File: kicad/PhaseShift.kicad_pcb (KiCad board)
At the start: 2 copper layers, 66.4 x 128.6 mm, 56 parts

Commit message: small tweak
- pogo pin
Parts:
- moved POGO1 0.12 mm to (175.1, 95.5)
- moved POGO2 0.12 mm to (233.9, 95.5)
- moved POGO3 0.12 mm to (175.1, 142.4)
- moved POGO4 0.12 mm to (233.9, 142.4)
- moved POGO5 0.12 mm to (175.1, 182.0)
- moved POGO6 0.12 mm to (233.9, 182.0)
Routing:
- net ROW12: track 180.7 -> 185.0 mm
- net COL0: track 172.6 -> 171.7 mm
- net ROW14: track 137.8 -> 138.5 mm
- net COL2: track 176.9 -> 176.3 mm
- net GND: vias 2 -> 6

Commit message: 202508.04
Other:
- board text added: "OmniCode:9001 - 202508.04"
- board text removed: "OmniCode:9001 - 202507.22"

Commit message: tweaked zone (#22)
* small tweak

* removed isolated copper islands
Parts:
- turned POGO1 to -90 degrees
- turned POGO2 to 90 degrees
- turned POGO3 to -90 degrees
- turned POGO4 to 90 degrees
- turned POGO5 to -90 degrees
- turned POGO6 to 90 degrees
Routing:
- net SCR: track 75.6 -> 71.4 mm
- net COL2: track 176.3 -> 178.8 mm, vias 3 -> 2
- net NUM: track 62.7 -> 64.7 mm
- net ROW12: track 185.0 -> 186.8 mm
- net Net-(L7-DIN): track 29.8 -> 31.5 mm
- net Net-(L10-DOUT): track 47.8 -> 46.2 mm
- net +5V: track 316.8 -> 317.9 mm, vias 4 -> 7
- net COL1: track 184.0 -> 184.9 mm
- net COL0: track 171.7 -> 172.6 mm
- net RGB_TO_RIGHT: track 44.8 -> 44.1 mm
- net Net-(D3-A): track 5.95 -> 5.44 mm
- net GND: vias 6 -> 7

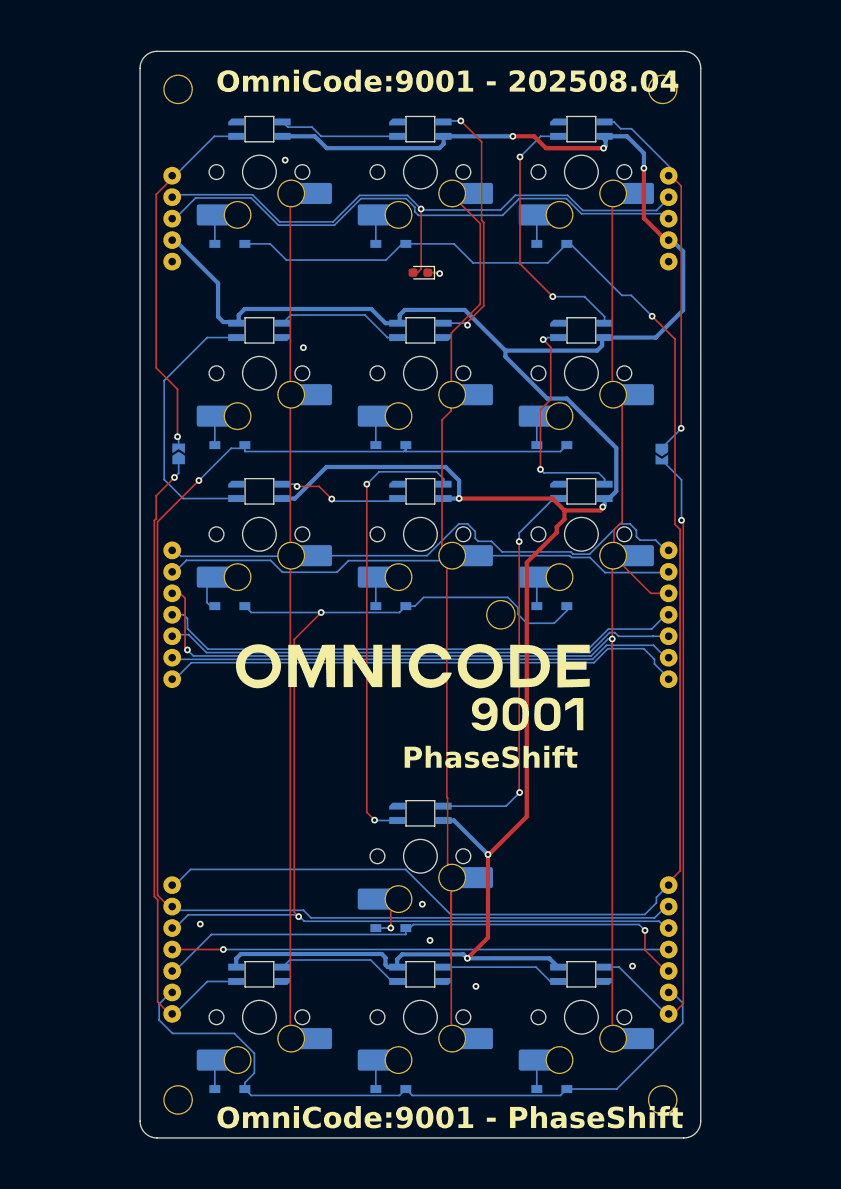
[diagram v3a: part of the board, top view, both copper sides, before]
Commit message: side bars
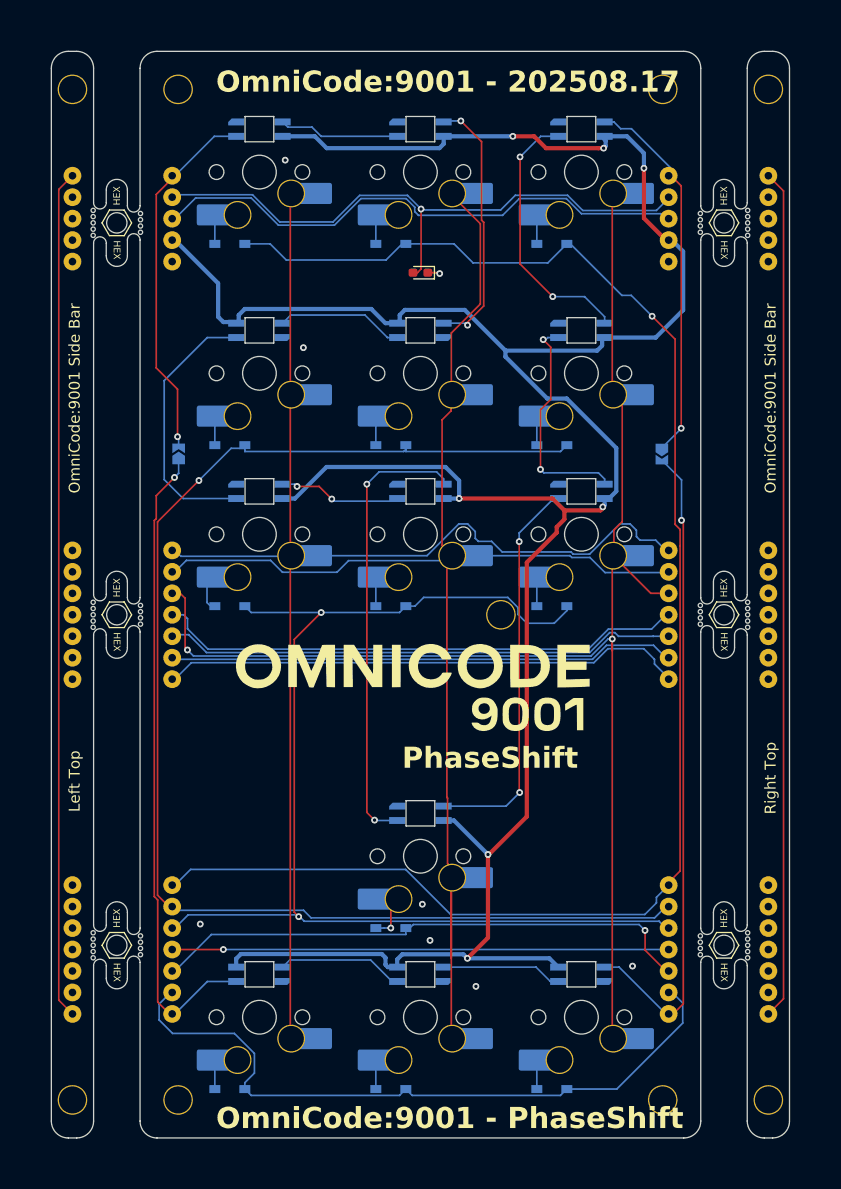
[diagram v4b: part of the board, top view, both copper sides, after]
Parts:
- added H6: MountingHole_3.2mm_Pad, TB2086_MISC:MountingHole_3.2mm_Pad, F.Cu at (163.3, 80.2)
- added H7: MountingHole_3.2mm_Pad, TB2086_MISC:MountingHole_3.2mm_Pad, F.Cu at (245.7, 80.2)
- added H8: MountingHole_3.2mm_Pad, TB2086_MISC:MountingHole_3.2mm_Pad, F.Cu at (163.3, 199.8)
- added H9: MountingHole_3.2mm_Pad, TB2086_MISC:MountingHole_3.2mm_Pad, F.Cu at (245.7, 199.8)
- added POGO10: Conn_01x07, TB2086_MISC:Pogopin_1x07_P2.54mm, F.Cu at (245.7, 142.4)
- added POGO11: Conn_01x07, TB2086_MISC:Pogopin_1x07_P2.54mm, F.Cu at (163.3, 182.0)
- added POGO12: Conn_01x07, TB2086_MISC:Pogopin_1x07_P2.54mm, F.Cu at (245.7, 182.0)
- added POGO7: Conn_01x05, TB2086_MISC:Pogopin_1x05_P2.54mm, F.Cu at (163.3, 95.5)
- added POGO8: Conn_01x05, TB2086_MISC:Pogopin_1x05_P2.54mm, F.Cu at (245.7, 95.5)
- added POGO9: Conn_01x07, TB2086_MISC:Pogopin_1x07_P2.54mm, F.Cu at (163.3, 142.4)
- added X1: 5.5mm, mousebites_5p5mm_easysnap, F.Cu at (171.3, 96.0)
- added X2: 5.5mm, mousebites_5p5mm_easysnap, F.Cu at (237.7, 96.0)
- added X3: 5.5mm, mousebites_5p5mm_easysnap, F.Cu at (171.3, 142.4)
- added X4: 5.5mm, mousebites_5p5mm_easysnap, F.Cu at (237.7, 142.4)
- added X5: 5.5mm, mousebites_5p5mm_easysnap, F.Cu at (171.3, 181.5)
- added X6: 5.5mm, mousebites_5p5mm_easysnap, F.Cu at (237.7, 181.5)
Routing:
- net RGB_RIGHT_SIDE: track 0.00 -> 100.7 mm
- net RGB_LEFT_SIDE: track 0.00 -> 100.5 mm
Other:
- board size 66.4 x 128.6 mm -> 87.4 x 128.6 mm
- board text added: "Left Top"
- board text added: "OmniCode:9001 - 202508.17"
- board text added: "OmniCode:9001 Side Bar"
- board text added: "Right Top"
- board text removed: "OmniCode:9001 - 202508.04"

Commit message: quick fix
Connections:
- POGO3 pad 5: COL4 -> COL6
- POGO3 pad 7: COL6 -> COL4
- POGO4 pad 1: COL6 -> COL4
- POGO4 pad 3: COL4 -> COL6
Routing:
- net COL6: track 61.9 -> 60.0 mm
- net COL4: track 60.0 -> 61.9 mm
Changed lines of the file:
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@@
 			(layers "*.Cu" "*.Mask")
 			(remove_unused_layers no)
-			(net 42 "COL4")
+			(net 41 "COL6")
 			(pinfunction "Pin_5")
 			(pintype "passive")
@@
 			(layers "*.Cu" "*.Mask")
 			(remove_unused_layers no)
-			(net 41 "COL6")
+			(net 42 "COL4")
 			(pinfunction "Pin_7")
 			(pintype "passive")
@@
 			(layers "*.Cu" "*.Mask")
 			(remove_unused_layers no)
-			(net 41 "COL6")
+			(net 42 "COL4")
 			(pinfunction "Pin_1")
 			(pintype "passive")
@@
 			(layers "*.Cu" "*.Mask")
 			(remove_unused_layers no)
-			(net 42 "COL4")
+			(net 41 "COL6")
 			(pinfunction "Pin_3")
 			(pintype "passive")
@@
 	)
 	(segment
-		(start 226.690079 146.401009)
-		(end 230.931009 146.401009)
+		(start 226.892637 144.5)
+		(end 224.532636 146.86)
 		(width 0.2)
 		(layer "B.Cu")
@@
 	)
 	(segment
-		(start 230.931009 146.401009)
-		(end 232.199 147.669)
+		(start 233.55 144.9275)
+		(end 232.065076 144.9275)
 		(width 0.2)
 		(layer "B.Cu")
@@
 	)
 	(segment
-		(start 225.031088 148.06)
-		(end 226.690079 146.401009)
+		(start 227.953298 144.94)
+		(end 227.953298 144.939339)
 		(width 0.2)
 		(layer "B.Cu")
@@
 	)
 	(segment
-		(start 177.3975 148.06)
-		(end 225.031088 148.06)
+		(start 232.065076 144.9275)
+		(end 232.052576 144.94)
 		(width 0.2)
 		(layer "B.Cu")
@@
 	)
 	(segment
-		(start 232.199 148.2065)
-		(end 234 150.0075)
+		(start 227.513959 144.5)
+		(end 226.892637 144.5)
 		(width 0.2)
 		(layer "B.Cu")
@@
 	)
 	(segment
-		(start 175.45 150.0075)
-		(end 177.3975 148.06)
+		(start 224.532636 146.86)
+		(end 179.19 146.86)
 		(width 0.2)
 		(layer "B.Cu")
@@
 	)
 	(segment
-		(start 232.199 147.669)
-		(end 232.199 148.2065)
+		(start 177.0718 144.7418)
+		(end 175.6357 144.7418)
 		(width 0.2)
 		(layer "B.Cu")
@@
 	)
 	(segment
-		(start 226.892637 144.5)
-		(end 224.532636 146.86)
+		(start 232.052576 144.94)
+		(end 227.953298 144.94)
 		(width 0.2)
 		(layer "B.Cu")
-		(net 42)
+		(net 41)
 	)
 	(segment
-		(start 233.55 144.9275)
-		(end 232.065076 144.9275)
+		(start 179.19 146.86)
+		(end 177.0718 144.7418)
 		(width 0.2)
 		(layer "B.Cu")
-		(net 42)
+		(net 41)
 	)
 	(segment
-		(start 227.953298 144.94)
-		(end 227.953298 144.939339)
+		(start 227.953298 144.939339)
+		(end 227.513959 144.5)
 		(width 0.2)
 		(layer "B.Cu")
-		(net 42)
+		(net 41)
 	)
 	(segment
-		(start 232.065076 144.9275)
-		(end 232.052576 144.94)
+		(start 226.690079 146.401009)
+		(end 230.931009 146.401009)
 		(width 0.2)
 		(layer "B.Cu")
@@
 	)
 	(segment
-		(start 227.513959 144.5)
-		(end 226.892637 144.5)
+		(start 230.931009 146.401009)
+		(end 232.199 147.669)
 		(width 0.2)
 		(layer "B.Cu")
@@
 	)
 	(segment
-		(start 224.532636 146.86)
-		(end 179.19 146.86)
+		(start 225.031088 148.06)
+		(end 226.690079 146.401009)
 		(width 0.2)
 		(layer "B.Cu")
@@
 	)
 	(segment
-		(start 177.0718 144.7418)
-		(end 175.6357 144.7418)
+		(start 177.3975 148.06)
+		(end 225.031088 148.06)
 		(width 0.2)
 		(layer "B.Cu")
@@
 	)
 	(segment
-		(start 232.052576 144.94)
-		(end 227.953298 144.94)
+		(start 232.199 148.2065)
+		(end 234 150.0075)
 		(width 0.2)
 		(layer "B.Cu")
@@
 	)
 	(segment
-		(start 179.19 146.86)
-		(end 177.0718 144.7418)
+		(start 175.45 150.0075)
+		(end 177.3975 148.06)
 		(width 0.2)
 		(layer "B.Cu")
@@
 	)
 	(segment
-		(start 227.953298 144.939339)
-		(end 227.513959 144.5)
+		(start 232.199 147.669)
+		(end 232.199 148.2065)
 		(width 0.2)
 		(layer "B.Cu")
